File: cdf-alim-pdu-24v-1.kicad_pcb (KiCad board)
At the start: 2 copper layers, 133 parts, among them J1 Conn_01x02, J10 Conn_01x02, J11 Conn_01x02, J12 Conn_01x02, J13 Conn_01x02, J14 Conn_01x02, J15 Conn_01x02, J16 Conn_01x02, J17 Conn_01x02, J2 Conn_01x02, J3 Conn_01x02, J4 Conn_01x02, J5 Conn_01x02, J6 Conn_01x02, J7 Conn_01x02, J8 Conn_01x02, J9 Conn_01x02, Q1 BSC019N04LS, Q2 BSC019N04LS, Q3 BSC019N04LS, U1 TPS25983, U2 TPS25983, U3 TPS25983, U4 HT753-1, U5 MX25947, U6 MX25947, U7 MX25947

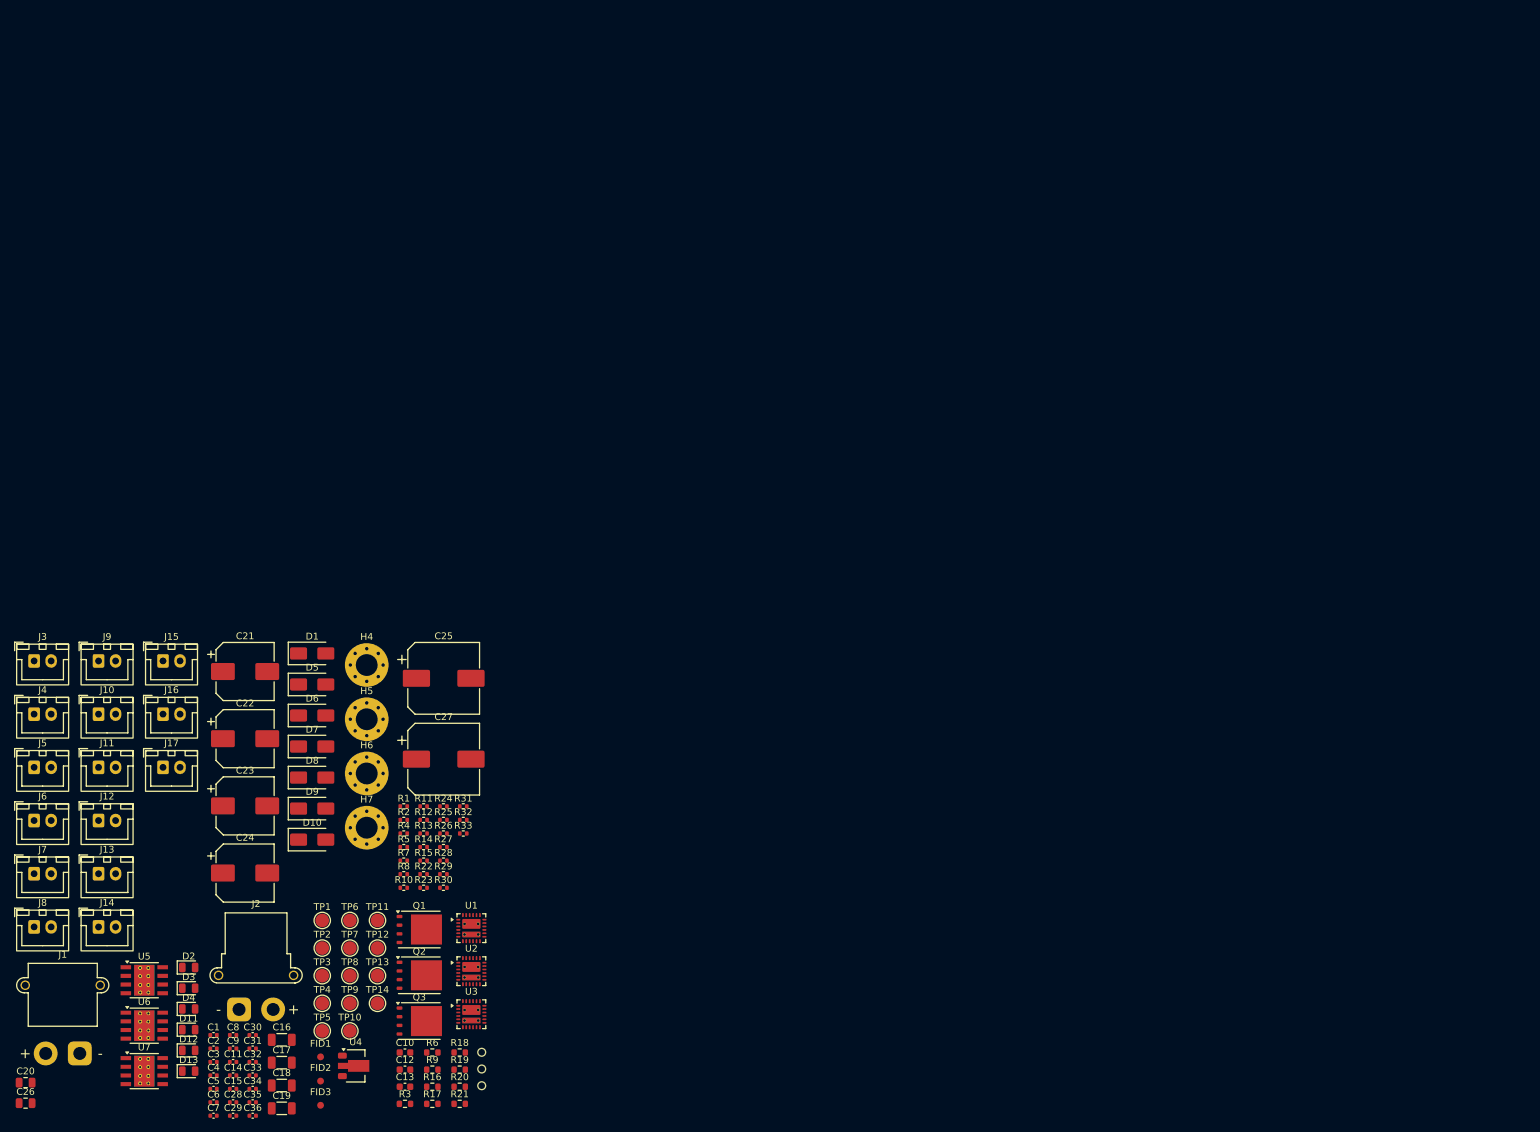
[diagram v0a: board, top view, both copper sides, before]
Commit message: pcb: add input efuse layout
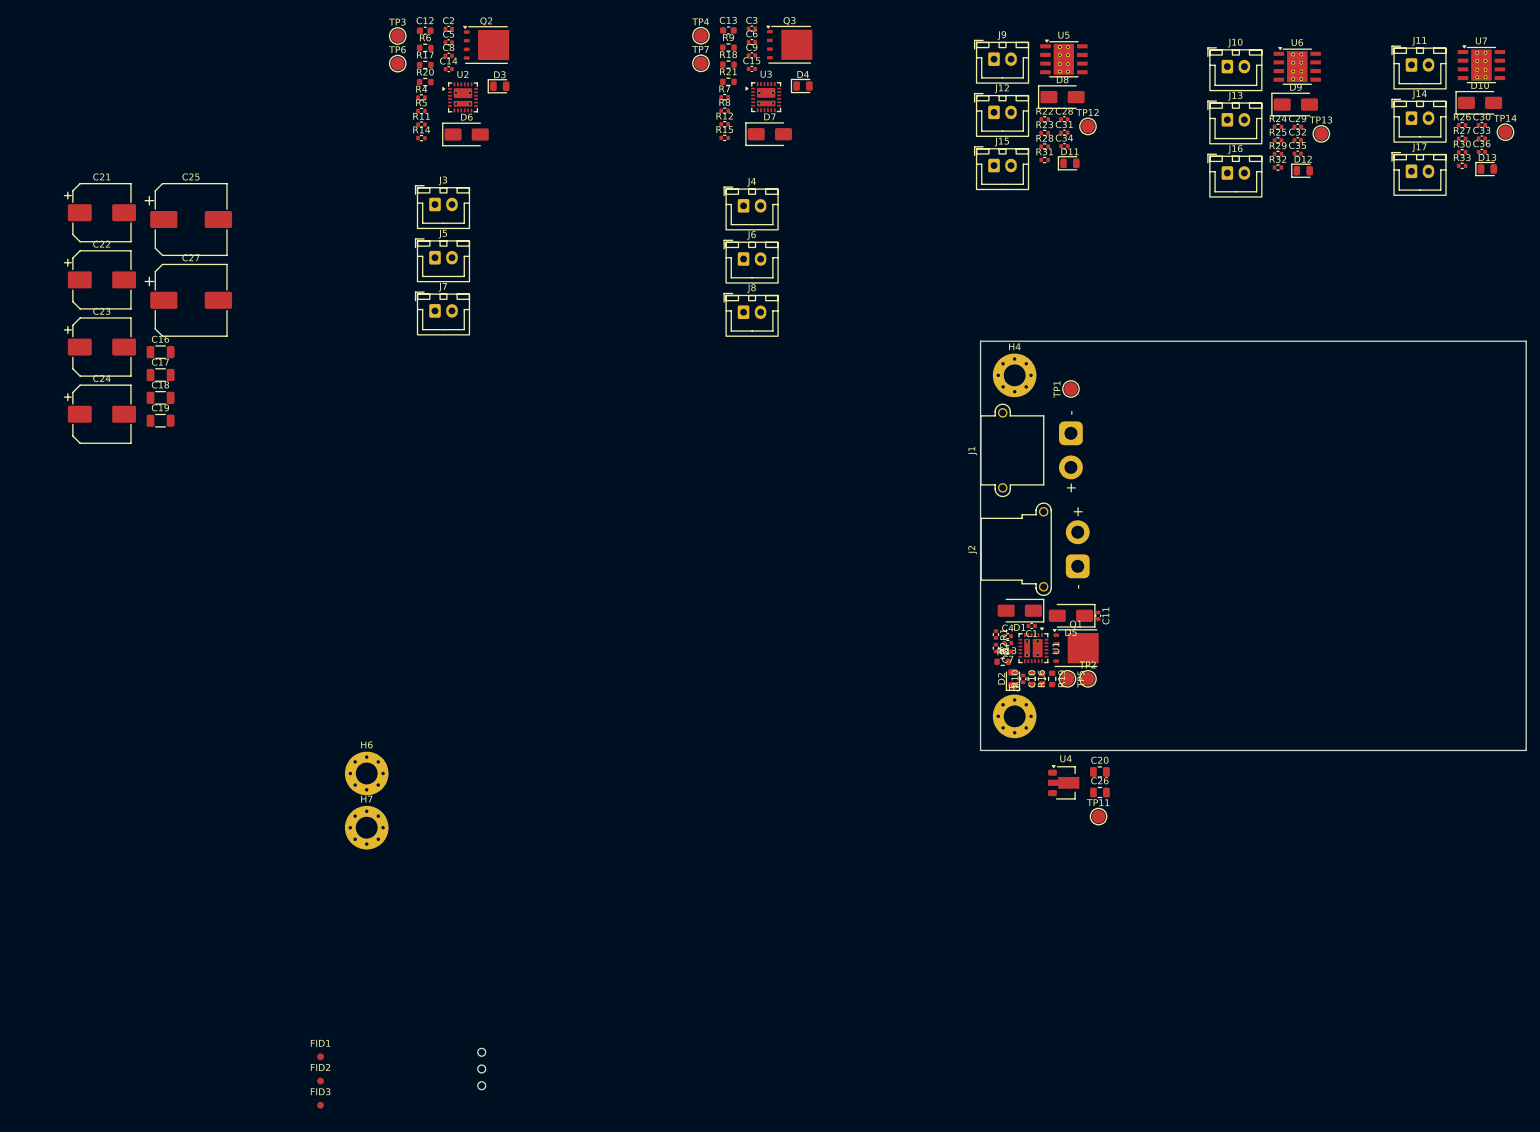
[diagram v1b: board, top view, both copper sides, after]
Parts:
- removed TP10, TP8, TP9: TestPoint, TestPoint:TestPoint_Pad_D2.0mm
- moved U7 245.4 mm to (233.4, 39.5)
- moved D13 231.8 mm to (234.3, 54.8)
- moved C36 229.0 mm to (233.5, 52.2)
- moved C33 226.6 mm to (233.5, 50.3)
- moved J14 226.1 mm to (223.2, 47.3)
- moved C30 224.2 mm to (233.5, 48.3)
- moved U6 219.9 mm to (206.4, 39.8)
- moved J11 218.3 mm to (223.2, 39.5)
- moved C29 213.1 mm to (206.5, 48.6)
- moved TP14 209.0 mm to (237.0, 49.3)
- moved D12 208.2 mm to (207.3, 55.0)
- moved C35 206.9 mm to (206.5, 52.5)
- moved C32 204.3 mm to (206.5, 50.5)
- moved J17 202.8 mm to (223.2, 55.1)
- moved D10 202.5 mm to (233.2, 45.0)
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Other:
- board outline added: 80 x 60 mm

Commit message: pcb: add ldo layout
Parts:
- moved C19 140.6 mm to (179.2, 73.8), turned to 90 degrees
- moved C16 135.1 mm to (174.8, 87.5), turned to 180 degrees
- moved C18 135.1 mm to (174.8, 82.5), turned to 180 degrees
- moved C17 135.0 mm to (174.8, 85.0), turned to 180 degrees
- moved C25 105.7 mm to (142.3, 101.7)
- moved C27 105.7 mm to (142.3, 113.5)
- moved C21 105.7 mm to (129.2, 100.7)
- moved C22 105.7 mm to (129.2, 110.5)
- moved C23 105.7 mm to (129.2, 120.3)
- moved C24 105.7 mm to (129.2, 130.2)
- moved C20 11.2 mm to (171.8, 133.5), turned to 90 degrees
- moved C26 10.8 mm to (171.8, 137.0), turned to -90 degrees
- moved U4 10.3 mm to (175.8, 135.0)
- moved TP1 3.50 mm to (169.8, 87.0)

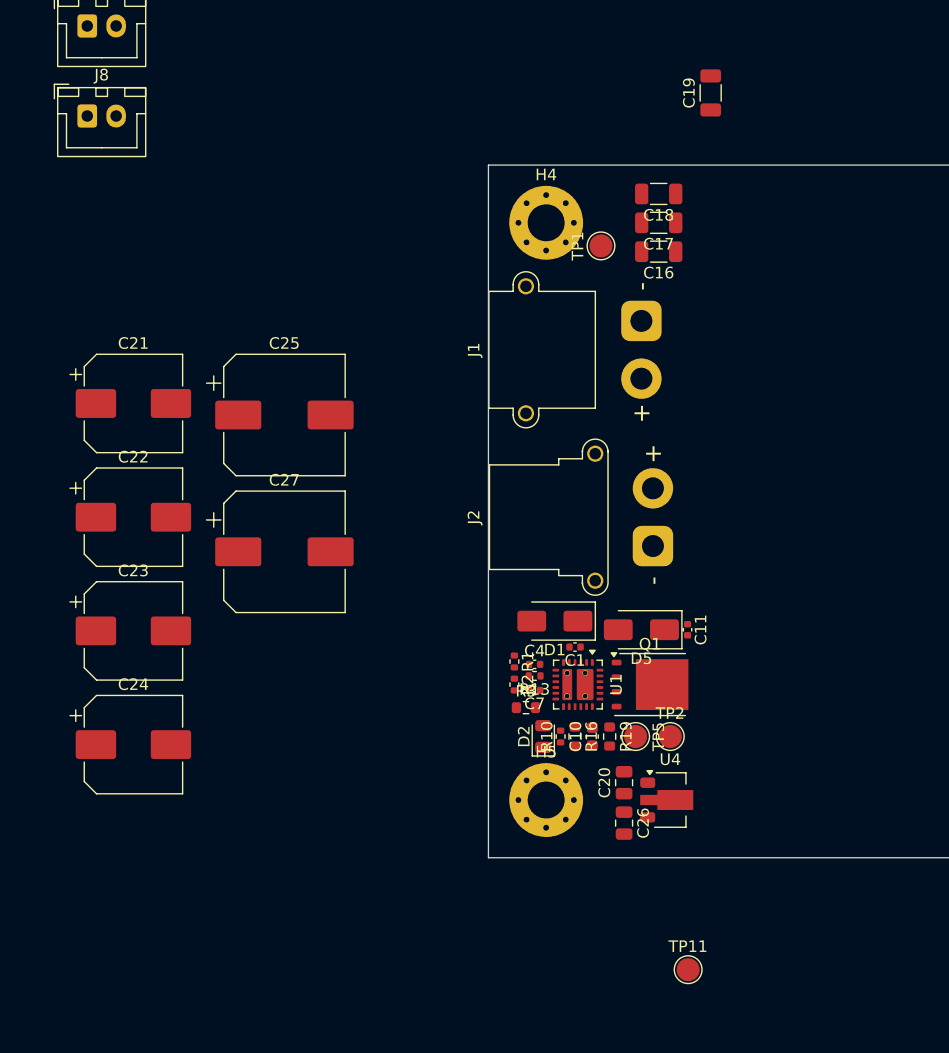
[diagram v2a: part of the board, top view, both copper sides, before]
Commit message: pcb: add decoupling caps layout
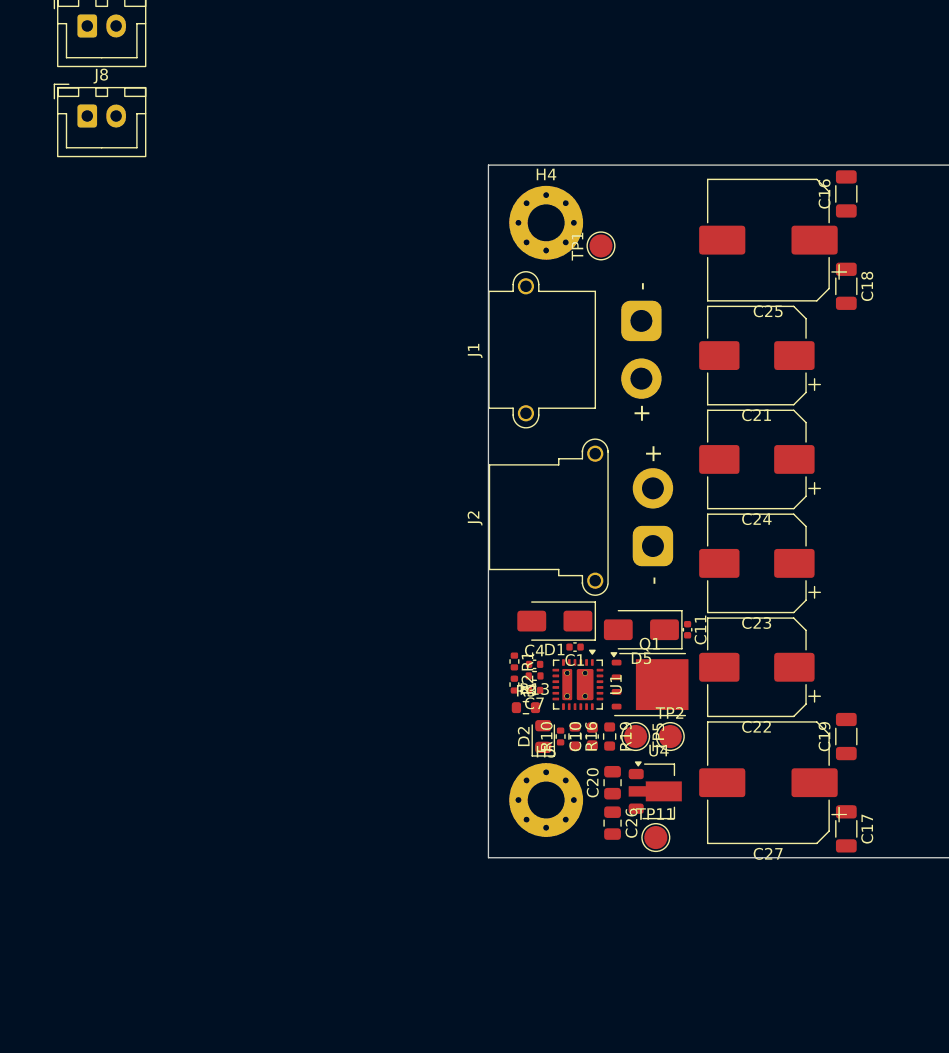
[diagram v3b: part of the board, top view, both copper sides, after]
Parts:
- moved C24 59.4 mm to (183.2, 105.5), turned to 180 degrees
- moved C19 57.0 mm to (191.0, 129.5)
- moved C22 55.5 mm to (183.2, 123.5), turned to 180 degrees
- moved C17 55.0 mm to (191.0, 137.5), turned to -90 degrees
- moved C23 54.3 mm to (183.2, 114.5), turned to 180 degrees
- moved C21 54.2 mm to (183.2, 96.5), turned to 180 degrees
- moved C27 46.4 mm to (184.2, 133.5), turned to 180 degrees
- moved C25 44.6 mm to (184.2, 86.5), turned to 180 degrees
- moved C18 18.1 mm to (191.0, 90.5), turned to -90 degrees
- moved C16 17.0 mm to (191.0, 82.5), turned to 90 degrees
- moved TP11 11.8 mm to (174.5, 138.2)
- moved U4 1.25 mm to (174.8, 134.2)
- moved C20 1.00 mm to (170.8, 133.5)
- moved C26 1.00 mm to (170.8, 137.0)

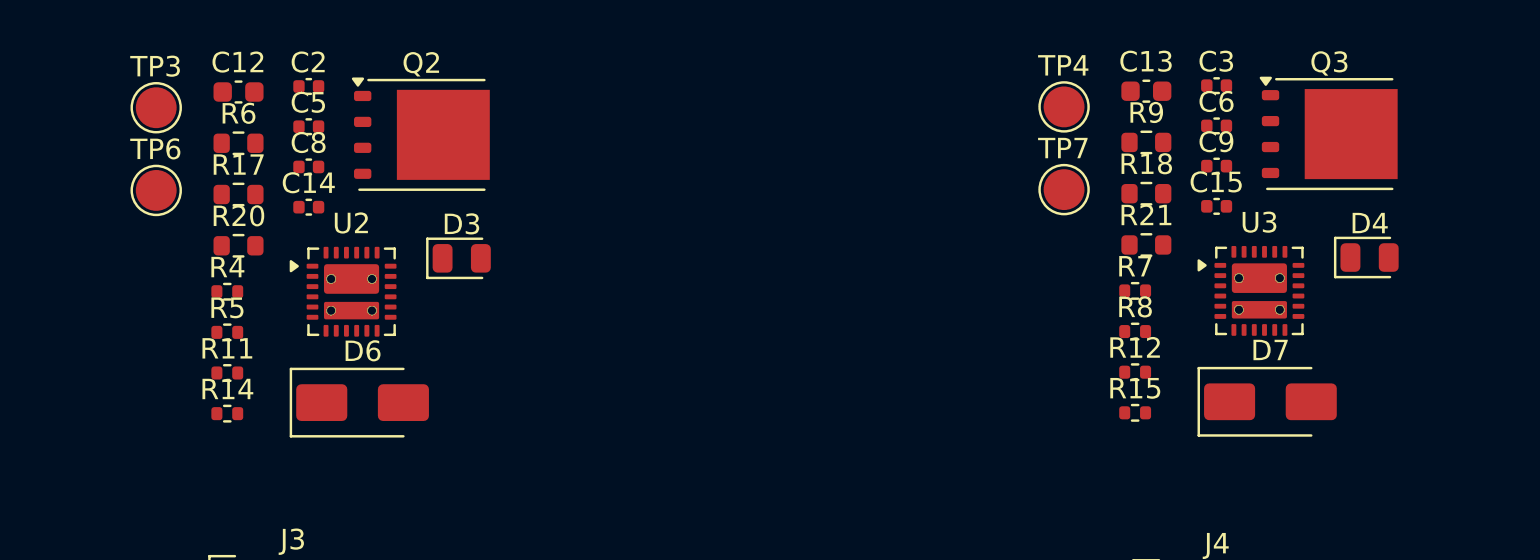
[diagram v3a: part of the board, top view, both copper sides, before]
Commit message: pcb: copy 8A efuse layout
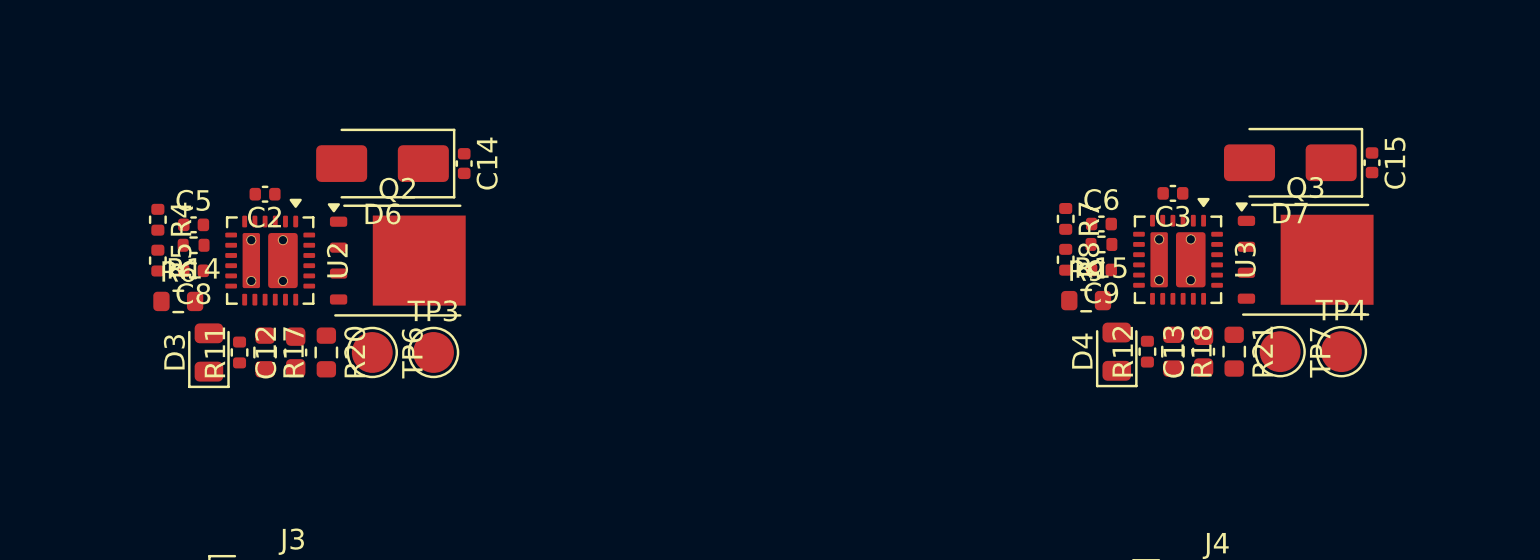
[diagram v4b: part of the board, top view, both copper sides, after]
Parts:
- moved TP4 18.1 mm to (132.6, 47.2)
- moved TP3 18.1 mm to (88.1, 47.2)
- moved TP7 13.2 mm to (129.6, 47.2), turned to -90 degrees
- moved TP6 13.2 mm to (85.1, 47.2), turned to -90 degrees
- moved D4 13.2 mm to (121.6, 47.2), turned to 90 degrees
- moved D3 13.2 mm to (77.1, 47.2), turned to 90 degrees
- moved C12 13.1 mm to (81.4, 47.2), turned to 90 degrees
- moved C13 13.1 mm to (125.8, 47.2), turned to 90 degrees
- moved D7 11.7 mm to (130.1, 37.9), turned to 180 degrees
- moved D6 11.7 mm to (85.6, 38.0), turned to 180 degrees
- moved R14 8.41 mm to (76.4, 42.0), turned to 180 degrees
- moved R15 8.41 mm to (120.8, 41.9), turned to 180 degrees
- moved R6 8.29 mm to (75.6, 44.7)
- moved R9 8.29 mm to (120.1, 44.7)
- moved C15 7.90 mm to (134.1, 37.9), turned to -90 degrees
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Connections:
- C1 pad 1: +24V_IN -> Net-(C1-Pad1)
- C2 pad 1: +24V -> Net-(C2-Pad1)
- C3 pad 1: +24V -> Net-(C3-Pad1)
- D1 pad 1: +24V_IN -> Net-(D1-A1)
- J1 pad 2: +24V_IN -> Net-(D1-A1)
- J2 pad 2: +24V_IN -> Net-(D1-A1)
- R1 pad 1: +24V_IN -> Net-(C1-Pad1)
- R4 pad 1: +24V -> Net-(C2-Pad1)
- R7 pad 1: +24V -> Net-(C3-Pad1)
- TP1 pad 1: +24V_IN -> Net-(D1-A1)
- U1 pad 1: +24V_IN -> Net-(C1-Pad1)
- U1 pad 16: +24V_IN -> Net-(C1-Pad1)
- U1 pad 2: +24V_IN -> Net-(C1-Pad1)
- U1 pad 25: +24V_IN -> Net-(C1-Pad1)
- U1 pad 3: +24V_IN -> Net-(C1-Pad1)
- U2 pad 1: +24V -> Net-(C2-Pad1)
- U2 pad 16: +24V -> Net-(C2-Pad1)
- U2 pad 2: +24V -> Net-(C2-Pad1)
- U2 pad 25: +24V -> Net-(C2-Pad1)
- U2 pad 3: +24V -> Net-(C2-Pad1)
- U3 pad 1: +24V -> Net-(C3-Pad1)
- U3 pad 16: +24V -> Net-(C3-Pad1)
- U3 pad 2: +24V -> Net-(C3-Pad1)
- U3 pad 25: +24V -> Net-(C3-Pad1)
- U3 pad 3: +24V -> Net-(C3-Pad1)
